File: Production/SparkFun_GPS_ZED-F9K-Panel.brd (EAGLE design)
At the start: 106 x 185.9 mm, 894 parts, among them J1 QWIIC_RIGHT_ANGLE, J10 QWIIC_RIGHT_ANGLE, J13 QWIIC_RIGHT_ANGLE, J16 QWIIC_RIGHT_ANGLE, J19 QWIIC_RIGHT_ANGLE, J22 QWIIC_RIGHT_ANGLE, J25 QWIIC_RIGHT_ANGLE, J28 QWIIC_RIGHT_ANGLE, J3 QWIIC_RIGHT_ANGLE, J31 QWIIC_RIGHT_ANGLE, J34 QWIIC_RIGHT_ANGLE, J4 QWIIC_RIGHT_ANGLE, U1 DUAL-OPTO_HCPL-073LSOIC-8, U10 UHS_INVERTER_SCHMITT_TRIGGERS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, U11 3.3V, U12 U-BLOX_ZED_F9K, U13 DUAL-OPTO_HCPL-073LSOIC-8, U14 UHS_INVERTER_SCHMITT_TRIGGERS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, U15 UHS_INVERTER_SCHMITT_TRIGGERS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, U16 3.3V, U17 U-BLOX_ZED_F9K, U18 DUAL-OPTO_HCPL-073LSOIC-8, U19 UHS_INVERTER_SCHMITT_TRIGGERS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, U2 U-BLOX_ZED_F9K, U20 UHS_INVERTER_SCHMITT_TRIGGERS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, U21 3.3V, U22 U-BLOX_ZED_F9K, U23 DUAL-OPTO_HCPL-073LSOIC-8, U24 UHS_INVERTER_SCHMITT_TRIGGERS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, U25 UHS_INVERTER_SCHMITT_TRIGGERS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, U26 3.3V, U27 U-BLOX_ZED_F9K, U28 DUAL-OPTO_HCPL-073LSOIC-8, U29 UHS_INVERTER_SCHMITT_TRIGGERS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, U3 UHS_INVERTER_SCHMITT_TRIGGERS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, U30 UHS_INVERTER_SCHMITT_TRIGGERS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, U4 UHS_INVERTER_SCHMITT_TRIGGERS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, U5 3.3V, U6 3.3V, U7 U-BLOX_ZED_F9K, U8 DUAL-OPTO_HCPL-073LSOIC-8, U9 UHS_INVERTER_SCHMITT_TRIGGERS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

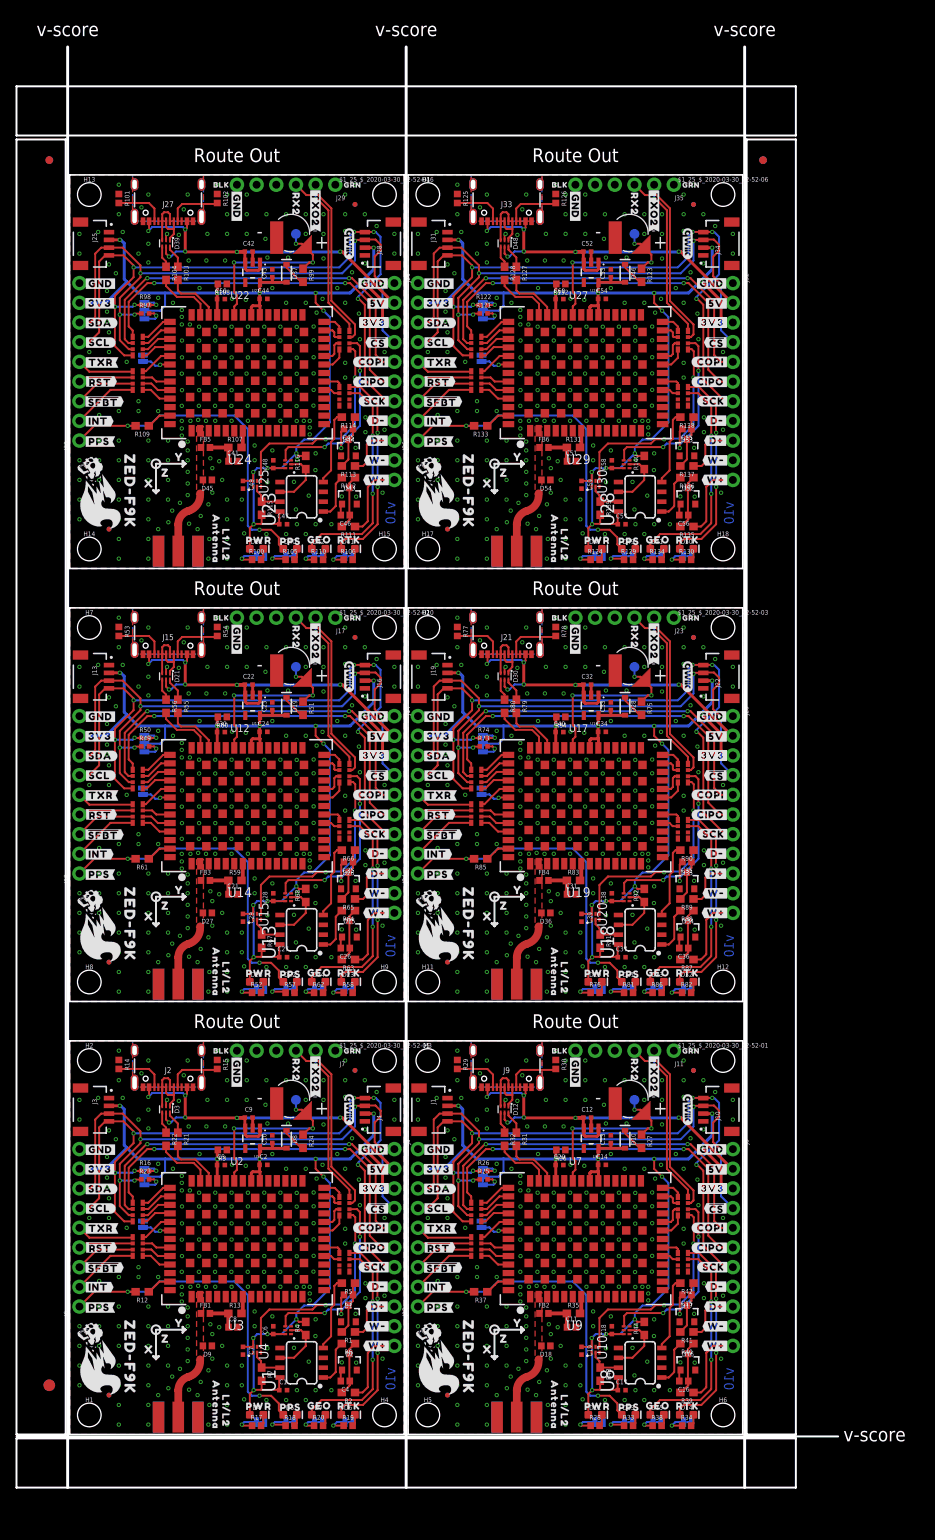
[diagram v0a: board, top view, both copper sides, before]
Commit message: Re-panelizes after silk change
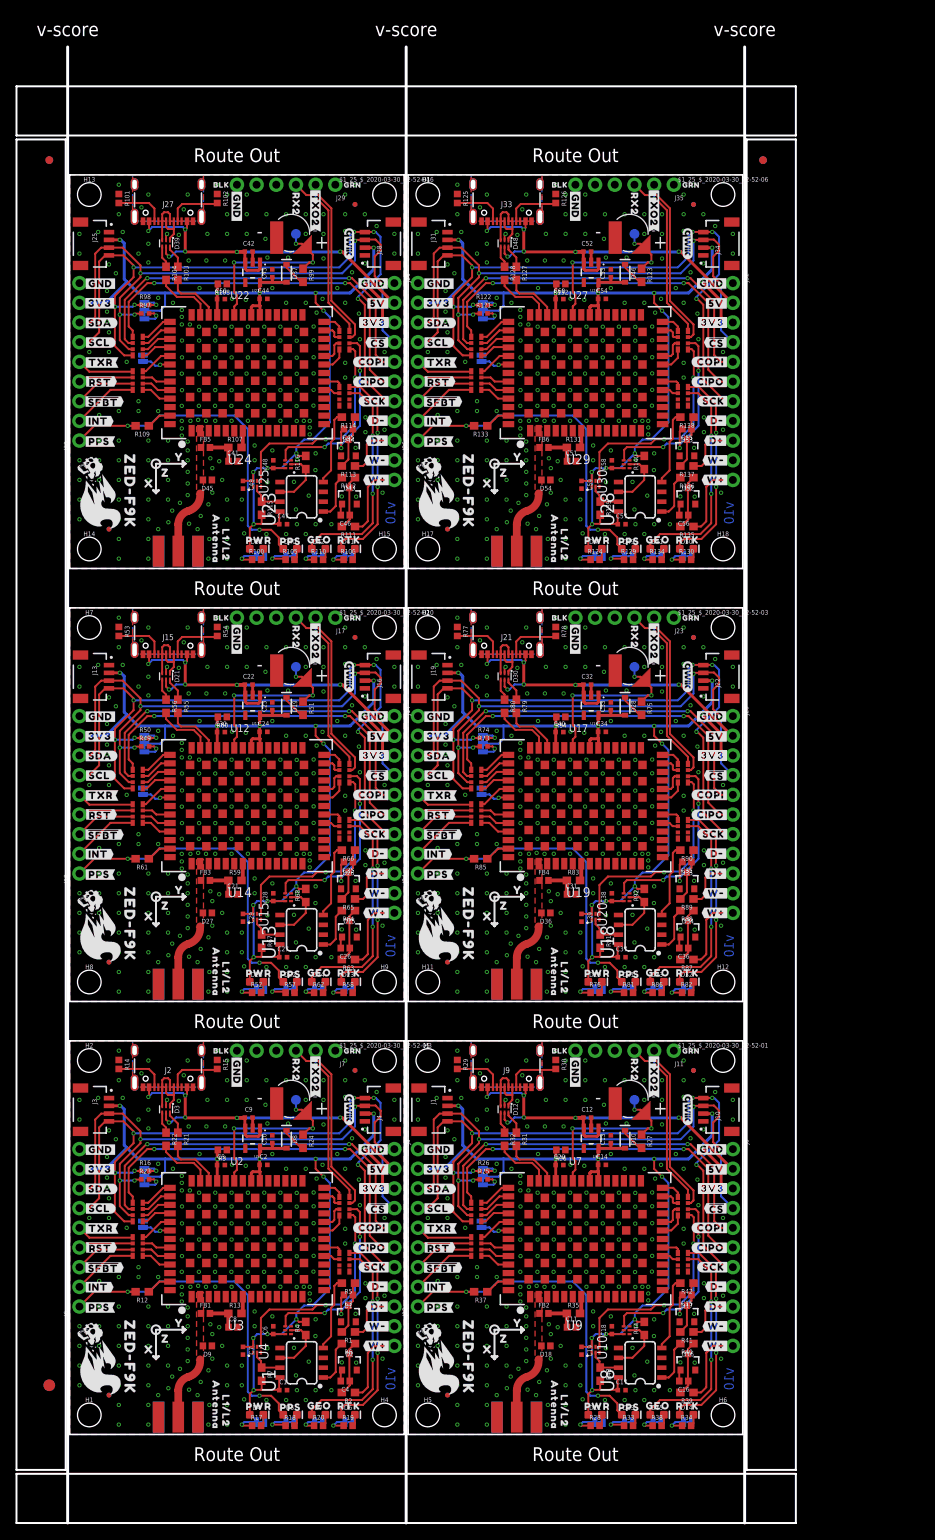
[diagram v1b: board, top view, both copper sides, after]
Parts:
- U$115, U$188, U$261, U$334, U$407: device silkbot:#TXO#COPI#9 -> silkbot:#SCL#SCK#12
- U$116, U$189, U$262, U$335, U$408: device silkbot:#SCL#SCK#12 -> silkbot:#D##6
- U$117, U$190, U$263, U$336, U$409: device silkbot:#D##6 -> silkbot:#D##7
- U$118, U$191, U$264, U$337, U$410: device silkbot:#D##7 -> silkbot:#W##4
- U$119, U$192, U$265, U$338, U$411: device silkbot:#W##4 -> silkbot:#W##5
- U$120, U$193, U$266, U$339, U$412: device silkbot:#W##5 -> silk:#GND#0
- U$121, U$194, U$267, U$340, U$413: device silk:#GND#0 -> silk:#3V3#6
- U$122, U$195, U$268, U$341, U$414: device silk:#3V3#6 -> silk:#SDA#6
- U$123, U$196, U$269, U$342, U$415: device silk:#SDA#6 -> silk:#SCL#7
- U$124, U$197, U$270, U$343, U$416: device silk:#SCL#7 -> silkbot:#TXR#3
- U$125, U$198, U$271, U$344, U$417: device silkbot:#TXR#3 -> silkbot:##RST##16
- U$126, U$199, U$272, U$345, U$418: device silkbot:##RST##16 -> silkbot:##SFBT##17
- U$127, U$200, U$273, U$346, U$419: device silkbot:##SFBT##17 -> silk:#INT#8
- U$128, U$201, U$274, U$347, U$420: device silk:#INT#8 -> silkbot:#PPS#0
- U$129, U$202, U$275, U$348, U$421: device silkbot:#PPS#0 -> silk:#RTK#25
- U$130, U$203, U$276, U$349, U$422: device silk:#RTK#25 -> silk:#GEO#24
- U$131, U$204, U$277, U$350, U$423: device silk:#GEO#24 -> silk:#PPS#21
- U$132, U$205, U$278, U$351, U$424: device silk:#PPS#21 -> silk:#PWR#23
- U$133, U$206, U$279, U$352, U$425: device silk:#PWR#23 -> silk:#SPI#22
- U$134, U$207, U$280, U$353, U$426: device silk:#SPI#22 -> silk:#I2C#23
- U$135, U$208, U$281, U$354, U$427: device silk:#I2C#23 -> silk:#RXI2#227
- U$136, U$209, U$282, U$355, U$428: device silk:#RXI2#227 -> silkbot:#TXO2#1
- U$137, U$210, U$283, U$356, U$429: device silkbot:#TXO2#1 -> silk:#GND#0
- U$138, U$211, U$284, U$357, U$430: device silk:#GND#0 -> silk:BLK227
- U$139, U$212, U$285, U$358, U$431: device silk:BLK227 -> silk:GRN228
- U$140, U$213, U$286, U$359, U$432: device silk:GRN228 -> silk:GNSS#DEAD_RECKONING230
- U$141, U$214, U$287, U$360, U$433: device silk:GNSS#DEAD_RECKONING230 -> silk:ZED#F9K230
- U$142, U$215, U$288, U$361, U$434: device silk:ZED#F9K230 -> silk:L1#L2229
- U$143, U$216, U$289, U$362, U$435: device silk:L1#L2229 -> silk:ANTENNA229
- U$144, U$217, U$290, U$363, U$436: device silk:ANTENNA229 -> silk:ZED#F9K230
- U$145, U$218, U$291, U$364, U$437: device silk:ZED#F9K230 -> silk:#PPS#20
- U$146, U$219, U$292, U$365, U$438: device silk:#PPS#20 -> silkbot:#TXO#CIPO#9
- U$29: device silkbot:#TXO#COPI#9 -> Dead#Reckoning#GPS#board#silk#FINAL#png:DEAD#RECKONING#GPS#BOARD#SILK#FINAL#JPG
- U$74: device Dead#Reckoning#GPS#board#silk#FINAL#png:DEAD#RECKONING#GPS#BOARD#SILK#FINAL#JPG -> silkbot:#TXO#CIPO#9
- moved U$193 42.4 mm to (3.97, 92.7)
- moved U$266 42.4 mm to (47.7, 92.7)
- moved U$120 42.4 mm to (47.7, 36.8)
- moved U$339 42.4 mm to (3.97, 148.5)
- moved U$412 42.4 mm to (47.7, 148.5)
- moved U$359 41.0 mm to (22.1, 122.8)
- moved U$432 41.0 mm to (65.8, 122.8)
- moved U$140 41.0 mm to (65.8, 11.1)
- moved U$213 41.0 mm to (22.1, 66.9)
- moved U$286 41.0 mm to (65.8, 66.9)
- moved U$129 34.8 mm to (79.7, 3.17)
- moved U$275 34.8 mm to (79.7, 59.0)
- moved U$202 34.8 mm to (36.0, 59.0)
- moved U$421 34.8 mm to (79.7, 114.9)
- moved U$348 34.8 mm to (36.0, 114.9)
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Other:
- board size 106 x 185.9 mm -> 100.6 x 190.5 mm

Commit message: Adds new panel from branch
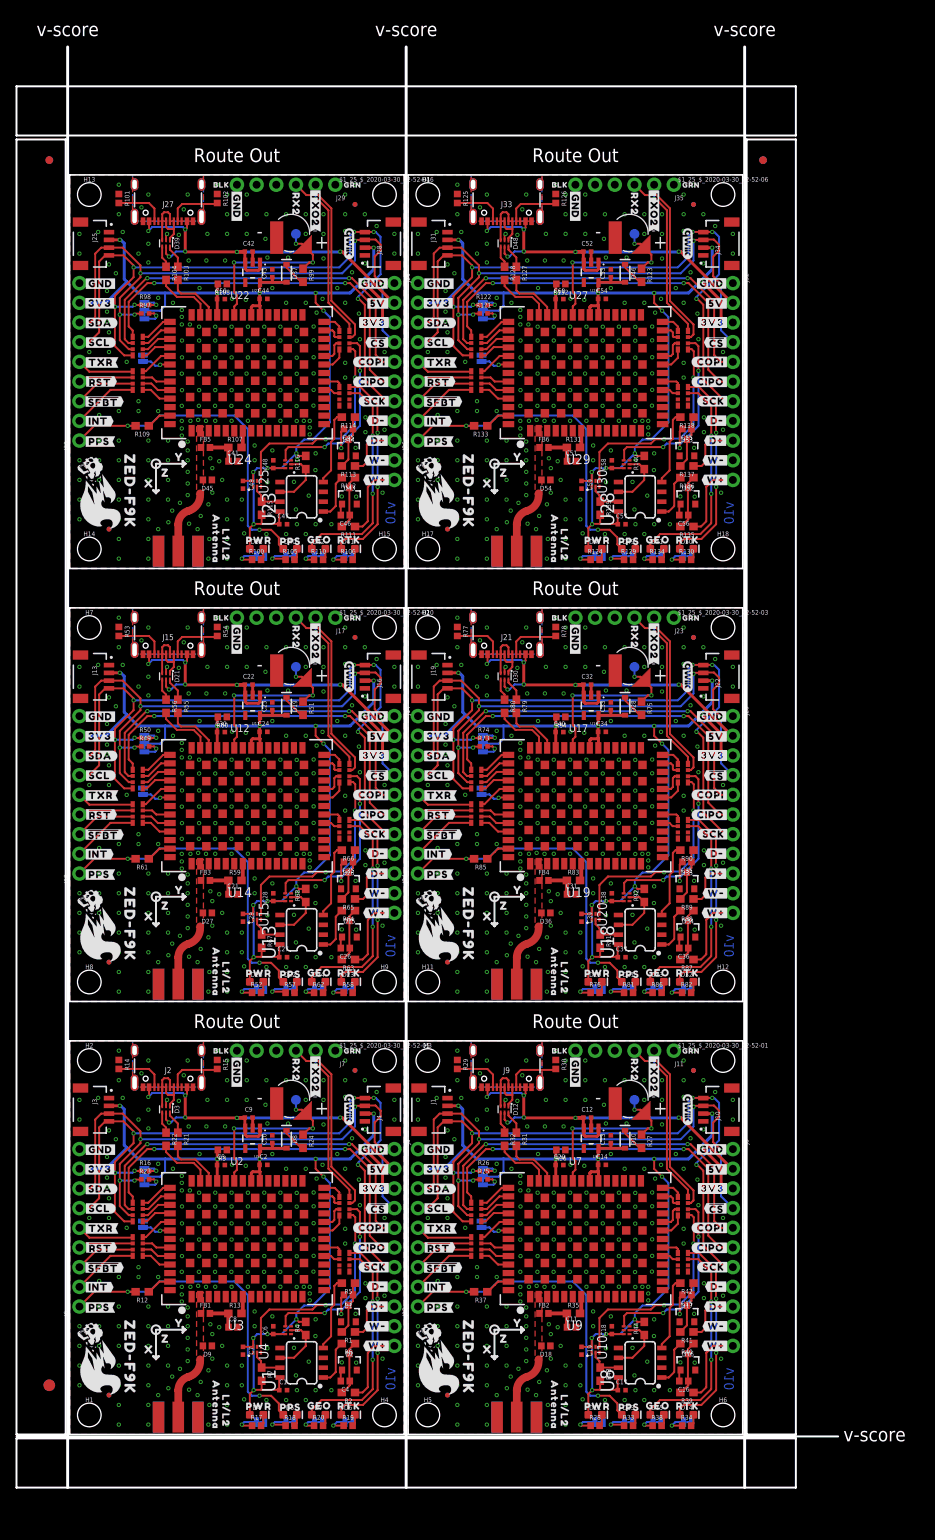
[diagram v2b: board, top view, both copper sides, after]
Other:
- board size 100.6 x 190.5 mm -> 106 x 185.9 mm
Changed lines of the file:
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@@
 <wire x1="8.2005875" y1="15.040409375" x2="9.0986125" y2="14.142384375" width="0.254" layer="22"/>
 <wire x1="9.046009375" y1="14.989609375" x2="8.147984375" y2="14.091584375" width="0.254" layer="22"/>
-<text x="21.59" y="-2.54" size="1.778" layer="20" ratio="15" align="center">Route Out</text>
 <wire x1="43.688" y1="0" x2="43.688" y2="50.8" width="0.2032" layer="20"/>
 <wire x1="43.688" y1="50.8" x2="86.868" y2="50.8" width="0.2032" layer="20"/>
@@
 <wire x1="51.8885875" y1="15.040409375" x2="52.7866125" y2="14.142384375" width="0.254" layer="22"/>
 <wire x1="52.734009375" y1="14.989609375" x2="51.835984375" y2="14.091584375" width="0.254" layer="22"/>
-<text x="65.278" y="-2.54" size="1.778" layer="20" ratio="15" align="center">Route Out</text>
 <wire x1="0" y1="55.88" x2="0" y2="106.68" width="0.2032" layer="20"/>
 <wire x1="0" y1="106.68" x2="43.18" y2="106.68" width="0.2032" layer="20"/>
@@
 <text x="65.278" y="109.22" size="1.778" layer="20" ratio="15" align="center">Route Out</text>
 <text x="65.278" y="165.1" size="1.778" layer="20" ratio="15" align="center">Route Out</text>
-<wire x1="-0.254" y1="-11.43" x2="-0.254" y2="179.07" width="0.381" layer="46"/>
+<wire x1="-0.254" y1="-6.858" x2="-0.254" y2="179.07" width="0.381" layer="46"/>
 <text x="-0.254" y="181.356" size="1.778" layer="46" ratio="15" align="center">v-score</text>
-<wire x1="43.434" y1="-11.43" x2="43.434" y2="179.07" width="0.381" layer="46"/>
+<wire x1="43.434" y1="-6.858" x2="43.434" y2="179.07" width="0.381" layer="46"/>
 <text x="43.434" y="181.356" size="1.778" layer="46" ratio="15" align="center">v-score</text>
-<wire x1="87.122" y1="-11.43" x2="87.122" y2="179.07" width="0.381" layer="46"/>
+<wire x1="87.122" y1="-6.858" x2="87.122" y2="179.07" width="0.381" layer="46"/>
 <text x="87.122" y="181.356" size="1.778" layer="46" ratio="15" align="center">v-score</text>
-<wire x1="-6.858" y1="-5.08" x2="93.726" y2="-5.08" width="0.254" layer="20"/>
-<wire x1="93.726" y1="-5.08" x2="93.726" y2="-11.43" width="0.254" layer="20"/>
-<wire x1="93.726" y1="-11.43" x2="-6.858" y2="-11.43" width="0.254" layer="20"/>
-<wire x1="-6.858" y1="-11.43" x2="-6.858" y2="-5.08" width="0.254" layer="20"/>
+<wire x1="-6.858" y1="-0.508" x2="93.726" y2="-0.508" width="0.254" layer="20"/>
+<wire x1="93.726" y1="-0.508" x2="93.726" y2="-6.858" width="0.254" layer="20"/>
+<wire x1="93.726" y1="-6.858" x2="-6.858" y2="-6.858" width="0.254" layer="20"/>
+<wire x1="-6.858" y1="-6.858" x2="-6.858" y2="-0.508" width="0.254" layer="20"/>
 <wire x1="87.376" y1="167.132" x2="93.726" y2="167.132" width="0.254" layer="20"/>
-<wire x1="93.726" y1="167.132" x2="93.726" y2="-4.572" width="0.254" layer="20"/>
-<wire x1="93.726" y1="-4.572" x2="87.376" y2="-4.572" width="0.254" layer="20"/>
-<wire x1="87.376" y1="-4.572" x2="87.376" y2="167.132" width="0.254" layer="20"/>
+<wire x1="93.726" y1="167.132" x2="93.726" y2="0" width="0.254" layer="20"/>
+<wire x1="93.726" y1="0" x2="87.376" y2="0" width="0.254" layer="20"/>
+<wire x1="87.376" y1="0" x2="87.376" y2="167.132" width="0.254" layer="20"/>
 <wire x1="-6.858" y1="173.99" x2="93.726" y2="173.99" width="0.254" layer="20"/>
 <wire x1="93.726" y1="173.99" x2="93.726" y2="167.64" width="0.254" layer="20"/>
@@
 <wire x1="-6.858" y1="167.64" x2="-6.858" y2="173.99" width="0.254" layer="20"/>
 <wire x1="-6.858" y1="167.132" x2="-0.508" y2="167.132" width="0.254" layer="20"/>
-<wire x1="-0.508" y1="167.132" x2="-0.508" y2="-4.572" width="0.254" layer="20"/>
-<wire x1="-0.508" y1="-4.572" x2="-6.858" y2="-4.572" width="0.254" layer="20"/>
-<wire x1="-6.858" y1="-4.572" x2="-6.858" y2="167.132" width="0.254" layer="20"/>
+<wire x1="-0.508" y1="167.132" x2="-0.508" y2="0" width="0.254" layer="20"/>
+<wire x1="-0.508" y1="0" x2="-6.858" y2="0" width="0.254" layer="20"/>
+<wire x1="-6.858" y1="0" x2="-6.858" y2="167.132" width="0.254" layer="20"/>
+<wire x1="-6.858" y1="-0.254" x2="99.187" y2="-0.254" width="0.254" layer="46"/>
+<text x="103.886" y="0" size="1.778" layer="46" ratio="15" align="center">v-score</text>
 </plain>
 <attributes>
